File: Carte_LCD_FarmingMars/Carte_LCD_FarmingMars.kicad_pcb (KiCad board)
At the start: 2 copper layers, 85 x 60 mm, 22 parts

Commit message: annotations
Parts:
- removed OK: SW_DIP_x01, ENAC_robotique:SWITCH_DTSM31NV
- added SW1: SW_Push, ENAC_robotique:SWITCH_DTSM31NV, F.Cu at (122.9, 126.8)
- renumbered BUZZER to BZ1, C100n to C1, C10u to C2, C100n to C3, RGB to D2, TIRETTE to J2, UART to J3, UPDI to J4, R470 to R1, R470 to R4, SELECT to RV2, R330 to R_Buzz1, COLOR to SW2, RETURN to SW3, REGU to U1, ATTINY to U2
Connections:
- SW2 pad 1: B_IN -> COULEUR
- U2 pad 5: COULEUR -> B_IN
- U2 pad 7: B_IN -> COULEUR
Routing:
- net COULEUR: track 28.6 -> 26.4 mm
- net B_IN: track 26.4 -> 28.6 mm
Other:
- board text added: "ATTINY"
- board text added: "BUZZER"
- board text added: "C100n"
- board text added: "C10u"
- board text added: "COULEUR"
- board text added: "JLCJLCJLCJLC"
- board text added: "OK"
- board text added: "R330"
- board text added: "R470"
- board text added: "RETURN"
- board text added: "SELECT"
- board text added: "TIRETTE"
- board text added: "UART"
- board text added: "UPDI"

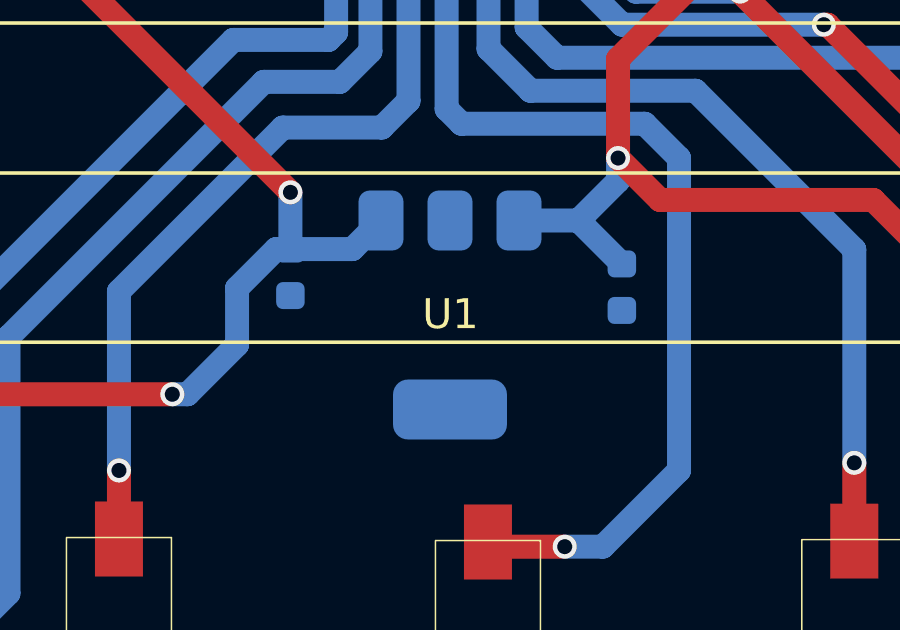
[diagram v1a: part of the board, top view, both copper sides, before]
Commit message: ajoute texte et marque pin1
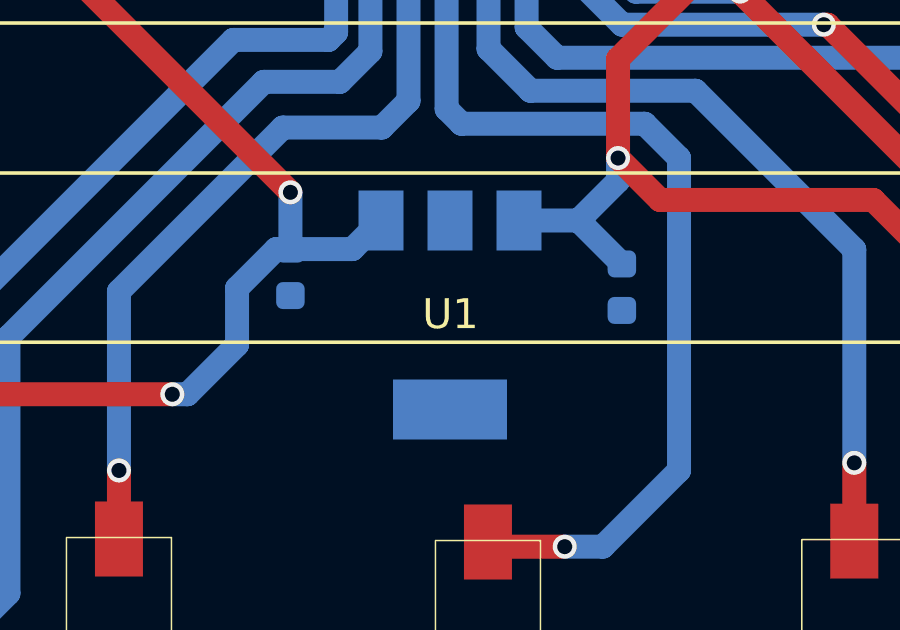
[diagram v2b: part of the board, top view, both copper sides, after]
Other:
- board text added: "5V_in"
- board text added: "RX"
- board text added: "TX"
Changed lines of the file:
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@@
 			)
 		)
-		(property ki_fp_filters "SOIC*7.5x12.8mm*P1.27mm*")
-		(sheetname "Racine")
-		(sheetfile "Carte_LCD_FarmingMars.kicad_sch")
 		(attr smd)
 		(fp_line
@@
 		)
 		(fp_line
+			(start -5.675 6.275)
+			(end -3.86 6.275)
+			(stroke
+				(width 0.12)
+				(type solid)
+			)
+			(layer "B.SilkS")
+		)
+		(fp_line
 			(start 3.86 6.51)
 			(end 0 6.51)
@@
 				(type solid)
 			)
-			(layer "B.SilkS")
-		)
-		(fp_poly
-			(pts
-				(xy -4.7125 6.275) (xy -5.0525 6.745) (xy -4.3725 6.745) (xy -4.7125 6.275)
-			)
-			(stroke
-				(width 0.12)
-				(type solid)
-			)
-			(fill solid)
 			(layer "B.SilkS")
 		)
@@
 			(pintype "power_in")
 		)
-		(model "${KICAD8_3DMODEL_DIR}/Package_SO.3dshapes/SOIC-20W_7.5x12.8mm_P1.27mm.wrl"
+		(model "${KICAD6_3DMODEL_DIR}/Package_SO.3dshapes/SOIC-20W_7.5x12.8mm_P1.27mm.wrl"
 			(offset
 				(xyz 0 0 0)
@@
 			)
 		)
-		(property ki_fp_filters "Converter*DCDC*RECOM*R*78E*0.5*")
-		(sheetname "Racine")
-		(sheetfile "Carte_LCD_FarmingMars.kicad_sch")
 		(attr smd)
 		(fp_line
 			(start 1.91 3.41)
-			(end -1.85 3.41)
+			(end -4.1 3.41)
 			(stroke
 				(width 0.12)
@@
 			(layer "B.SilkS")
 		)
-		(fp_poly
-			(pts
-				(xy -3.13 3.31) (xy -3.37 3.64) (xy -2.89 3.64) (xy -3.13 3.31)
-			)
-			(stroke
-				(width 0.12)
-				(type solid)
-			)
-			(fill solid)
-			(layer "B.SilkS")
-		)
 		(fp_line
 			(start -4.4 3.6)
@@
 		)
 		(fp_text user "${REFERENCE}"
-			(at 0 0 0)
+			(at 0 0 180)
 			(layer "B.Fab")
 			(effects
@@
 			)
 		)
-		(pad "1" smd roundrect
+		(pad "1" smd rect
 			(at -3.15 2.3 270)
 			(size 2 1.5)
 			(layers "B.Cu" "B.Paste" "B.Mask")
-			(roundrect_rratio 0.25)
 			(net 6 "+5V")
 			(pinfunction "IN")
 			(pintype "power_in")
 		)
-		(pad "2" smd roundrect
+		(pad "2" smd rect
 			(at -3.15 0 270)
 			(size 2 1.5)
 			(layers "B.Cu" "B.Paste" "B.Mask")
-			(roundrect_rratio 0.25)
 			(net 1 "GND")
 			(pinfunction "GND")
 			(pintype "power_in")
 		)
-		(pad "2" smd roundrect
+		(pad "2" smd rect
 			(at 3.15 0 270)
 			(size 2 3.8)
 			(layers "B.Cu" "B.Paste" "B.Mask")
-			(roundrect_rratio 0.25)
 			(net 1 "GND")
 			(pinfunction "GND")
 			(pintype "power_in")
 		)
-		(pad "3" smd roundrect
+		(pad "3" smd rect
 			(at -3.15 -2.3 270)
 			(size 2 1.5)
 			(layers "B.Cu" "B.Paste" "B.Mask")
-			(roundrect_rratio 0.25)
 			(net 2 "+3.3V")
 			(pinfunction "OUT")
 			(pintype "power_out")
 		)
-		(model "${KICAD8_3DMODEL_DIR}/Package_TO_SOT_SMD.3dshapes/SOT-223.wrl"
+		(model "${KICAD6_3DMODEL_DIR}/Package_TO_SOT_SMD.3dshapes/SOT-223.wrl"
 			(offset
 				(xyz 0 0 0)
@@
 		(layer "B.SilkS")
 	)
+	(gr_circle
+		(center 117.348 105.156)
+		(end 117.602 105.41)
+		(stroke
+			(width 0.15)
+			(type default)
+		)
+		(fill none)
+		(layer "B.SilkS")
+	)
 	(gr_rect
 		(start 78 75)
@@
 	(gr_text "C100n"
 		(at 104.648 117.348 90)
+		(layer "B.SilkS")
+		(effects
+			(font
+				(size 1 1)
+				(thickness 0.153)
+			)
+			(justify left bottom mirror)
+		)
+	)
+	(gr_text "5V_in"
+		(at 94.742 122.428 0)
+		(layer "B.SilkS")
+		(effects
+			(font
+				(size 1 1)
+				(thickness 0.153)
+			)
+			(justify left bottom mirror)
+		)
+	)
+	(gr_text "GND"
+		(at 90.424 108.712 0)
 		(layer "B.SilkS")
 		(effects
@@
 		)
 	)
+	(gr_text "TX"
+		(at 92.71 127.762 0)
+		(layer "B.SilkS")
+		(effects
+			(font
+				(size 1 1)
+				(thickness 0.153)
+			)
+			(justify left bottom mirror)
+		)
+	)
 	(gr_text "GND"
 		(at 90.551 97.917 0)
@@
 		)
 	)
+	(gr_text "RX"
+		(at 92.964 130.048 0)
+		(layer "B.SilkS")
+		(effects
+			(font
+				(size 1 1)
+				(thickness 0.153)
+			)
+			(justify left bottom mirror)
+		)
+	)
 	(gr_text "TIRETTE"
-		(at 90.678 108.712 0)
+		(at 90.932 100.838 0)
 		(layer "B.SilkS")
 		(effects
@@
 		(layer "B.SilkS")
 		(effects
+			(font
+				(size 1 1)
+				(thickness 0.153)
+			)
+			(justify left bottom mirror)
+		)
+	)
+	(gr_text "GND"
+		(at 93.98 124.968 0)
+		(layer "B.SilkS")
+		(effects
